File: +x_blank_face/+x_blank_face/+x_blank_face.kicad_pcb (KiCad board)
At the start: 2 copper layers, 87 x 326.5 mm, 25 parts, among them J1 Conn_01x08_Pin, J2 Conn_01x02_Pin, J3 Conn_01x02_Pin

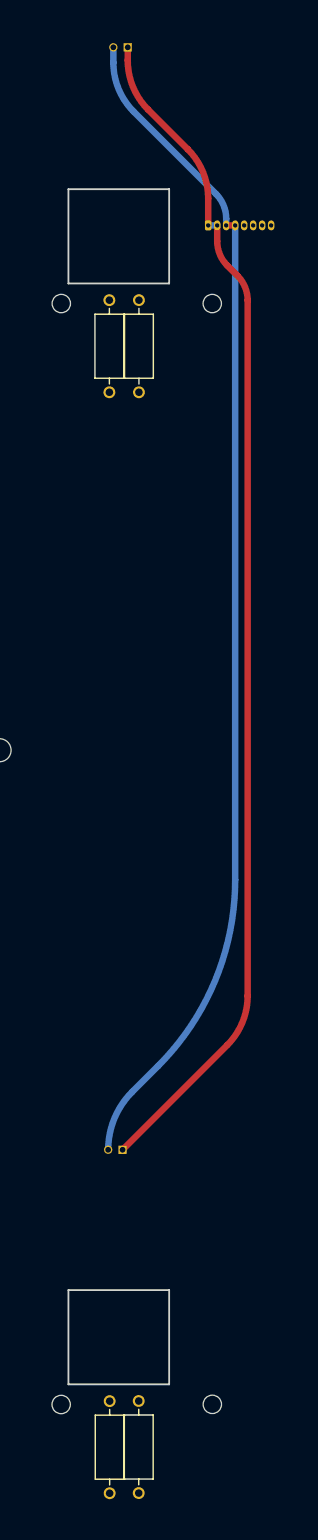
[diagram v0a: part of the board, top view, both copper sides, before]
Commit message: Updated +X blank to remove GND and PWR plane, and changed parallel switches to series switches
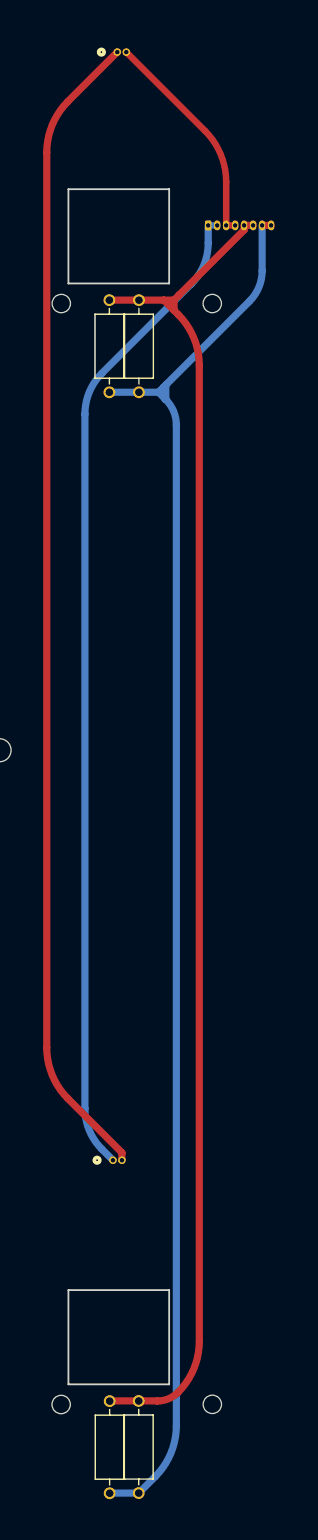
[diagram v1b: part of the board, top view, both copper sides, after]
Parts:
- J2, J3: footprint CNN_GNSS_Footprint:TE_440055-2 -> CNN_GNSS_Footprint:CON2_1X2_UR_DF13
- moved J2 1.97 mm to (173.7, 151.1)
- moved J3 1.60 mm to (174.3, -2.90)
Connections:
- J2 pad 2: /-X Serial Out -> Net-(J2-Pin_2)
- J3 pad 1: GND -> Net-(J2-Pin_2)
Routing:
- net /12VPDM: track 0.00 -> 200.1 mm
- net /+X Drain: track 0.49 -> 191.7 mm
- net Net-(J2-Pin_2): track 0.00 -> 161.4 mm
- net /-X Serial Out: track 165.3 -> 30.6 mm
- net GND: track 166.2 -> 138.7 mm

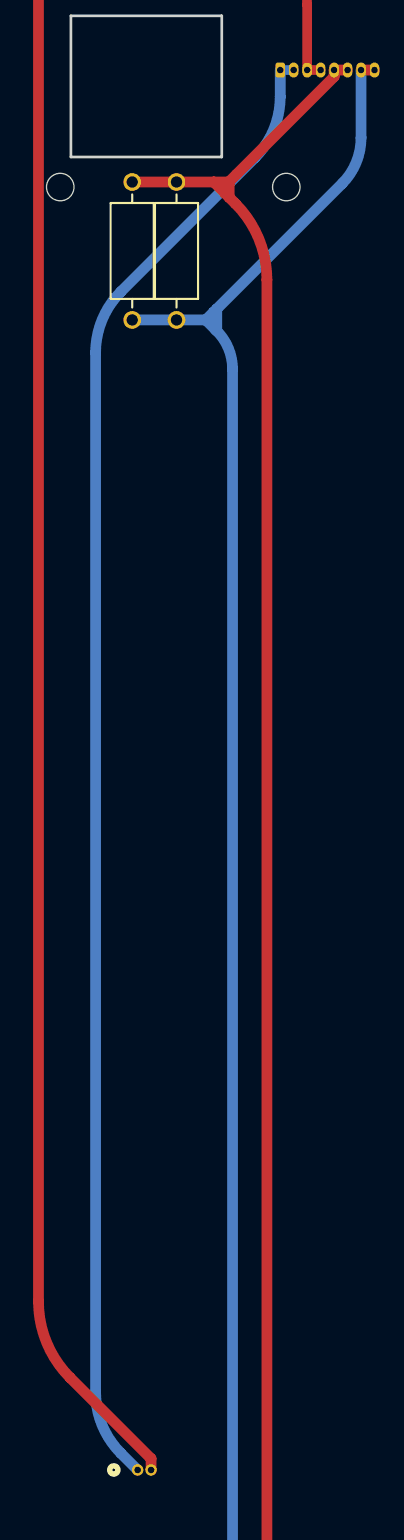
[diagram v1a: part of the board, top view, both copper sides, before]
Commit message: fixed 3d models for connectors
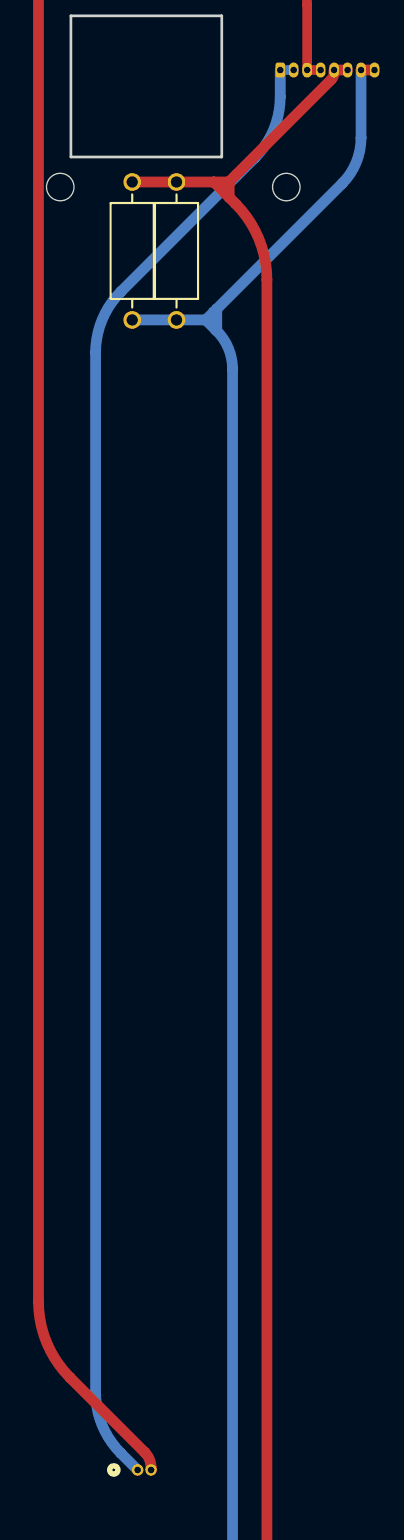
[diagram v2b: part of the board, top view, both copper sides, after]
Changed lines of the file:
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@@
 		(sheetname "/")
 		(sheetfile "+x_blank_face.kicad_sch")
-		(units
-			(unit
-				(name "A")
-				(pins "1" "2" "3" "4" "5" "6" "7" "8")
-			)
-		)
 		(attr smd)
 		(duplicate_pad_numbers_are_jumpers no)
@@
 			(pinfunction "Pin_1_1")
 			(pintype "passive")
-			(teardrops
-				(best_length_ratio 0.5)
-				(max_length 1)
-				(best_width_ratio 1)
-				(max_width 2)
-				(curved_edges yes)
-				(filter_ratio 0.9)
-				(enabled yes)
-				(allow_two_segments yes)
-				(prefer_zone_connections yes)
-			)
 		)
 		(pad "2" thru_hole oval
@@
 			(pinfunction "Pin_2_2")
 			(pintype "passive")
-			(teardrops
-				(best_length_ratio 0.5)
-				(max_length 1)
-				(best_width_ratio 1)
-				(max_width 2)
-				(curved_edges yes)
-				(filter_ratio 0.9)
-				(enabled yes)
-				(allow_two_segments yes)
-				(prefer_zone_connections yes)
-			)
 		)
 		(pad "3" thru_hole oval
@@
 		(model "C:/Users/hayla/Downloads/DF13-8P-1.25DSA(25)_CL0536-0107-5-25_3DDrawing_STEP_0001217332S/DF13-8P-1.25DSA.stp"
 			(offset
-				(xyz -11.55 -25.6 0)
+				(xyz -11.55 -25.6 1.5)
 			)
 			(scale
@@
 	)
 	(segment
-		(start 191.935 21.806346)
+		(start 191.642107 22.099239)
 		(end 182.870673 30.870673)
 		(width 1)
@@
 	(segment
 		(start 191.935 21.18)
-		(end 191.935 21.806346)
+		(end 191.935 21.392132)
 		(width 1)
 		(layer "F.Cu")
@@
 		(mid 181.41288 184.256518)
 		(end 179.882146 184.561)
+		(width 1)
+		(layer "F.Cu")
+		(net "/+X Drain")
+	)
+	(arc
+		(start 191.642107 22.099239)
+		(mid 191.85888 21.774816)
+		(end 191.935 21.392132)
 		(width 1)
 		(layer "F.Cu")
@@
 	(segment
 		(start 167.428932 142.528932)
-		(end 174.95 150.05)
+		(end 174.364214 149.464214)
 		(width 1)
 		(layer "F.Cu")
@@
 	)
 	(segment
-		(start 174.95 150.05)
+		(start 174.95 150.878427)
 		(end 174.95 151.1)
 		(width 1)
@@
 		(width 1)
 		(layer "F.Cu")
+		(net "Net-(J2-Pin_2)")
+	)
+	(arc
+		(start 174.95 150.878427)
+		(mid 174.797759 150.11306)
+		(end 174.364214 149.464214)
+		(width 1)
+		(layer "F.Cu")

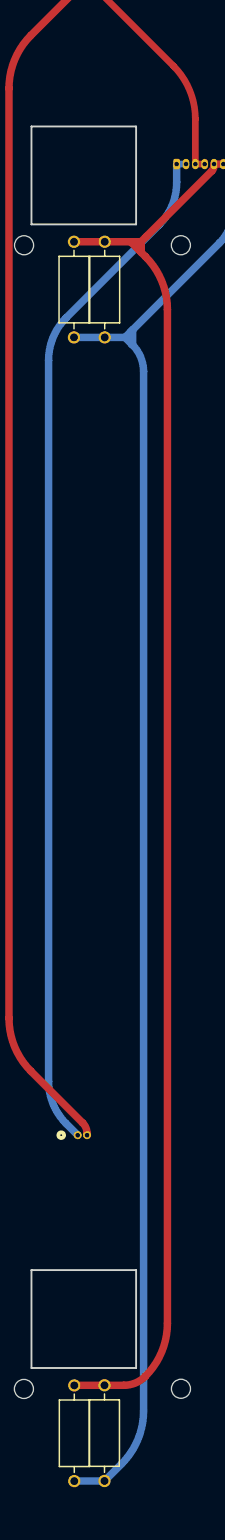
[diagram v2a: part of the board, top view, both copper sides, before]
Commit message: changed cover panels to have smaller power planes, also changed front panel DF13 from SMD to THT
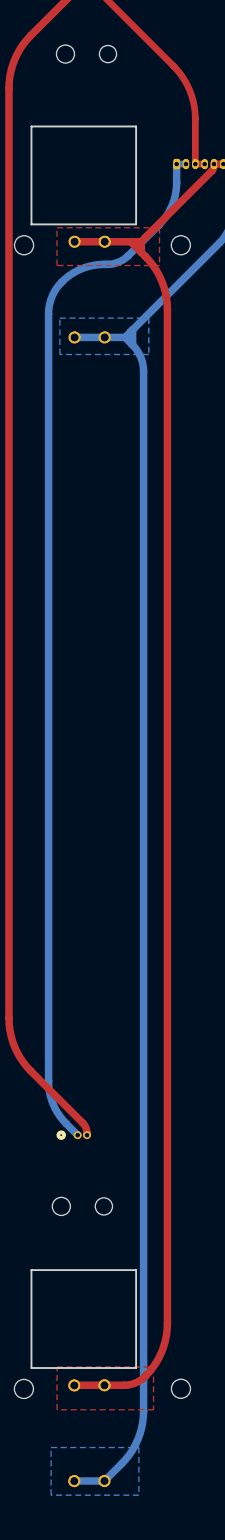
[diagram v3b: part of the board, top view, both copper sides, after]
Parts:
- moved R2 0.08 mm to (173.3, 44.4)
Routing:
- net GND: track 138.7 -> 141.4 mm
- added copper zone on F.Cu, net /+X Drain
- added copper zone on B.Cu, net /12VPDM
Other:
- outline, holes or cut-outs redrawn
